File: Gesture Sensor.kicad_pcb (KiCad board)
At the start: 2 copper layers, 25.4 x 17.8 mm, 18 parts, among them J1 Conn_01x06_Male, J2 SM04B-SRSS-TB(LF)(SN), J3 SM04B-SRSS-TB(LF)(SN), U1 APDS-9960

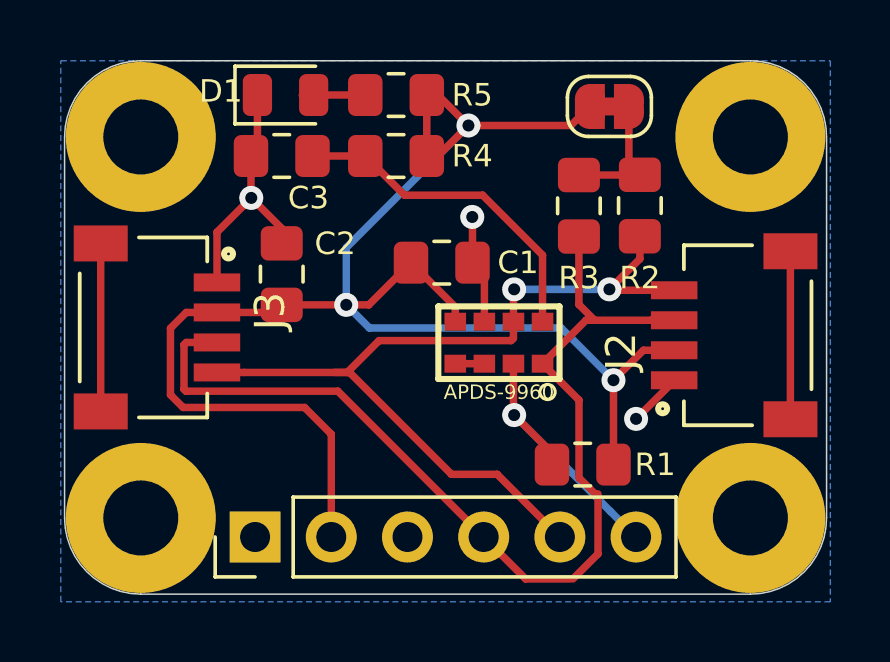
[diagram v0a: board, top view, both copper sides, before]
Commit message: Fixed schematic issue with Mosfet
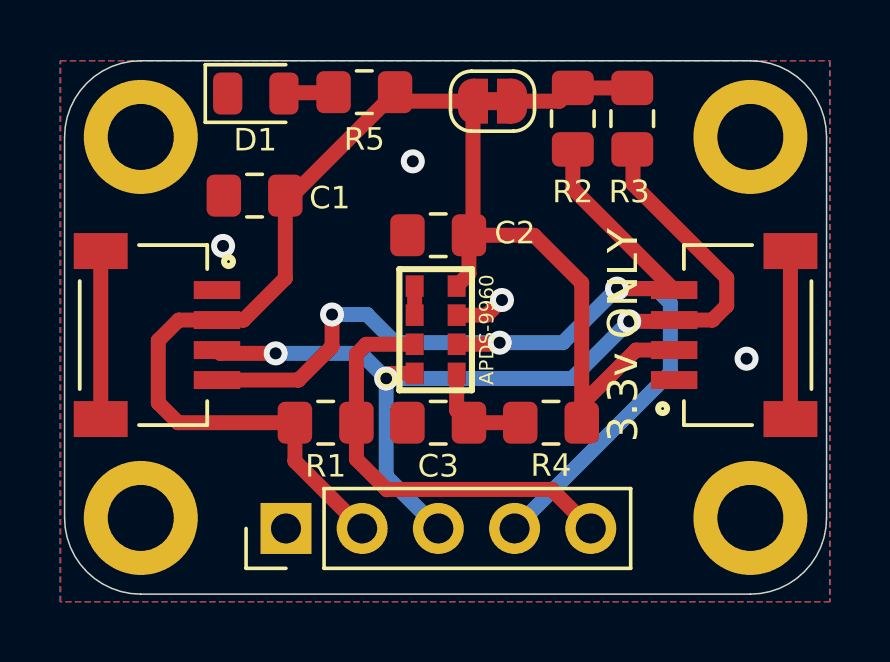
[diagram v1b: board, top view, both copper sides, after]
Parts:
- added G***: LOGO, Images:triplehorn_3-8_back_mask, F.Cu at (153.7, 54.1)
- added REF**: OSHW-Logo2_7.3x6mm_BackMask, Images:OSHW-Logo2_7.3x6mm_BackMask, F.Cu at (134.9, 55.4)
- H1, H2, H3, H4: footprint MountingHole:MountingHole_2.5mm_Pad -> MountingHole:MountingHole_2.2mm_M2_ISO14580_Pad
- J1: value Conn_01x06_Male -> Conn_01x05_Male; footprint Connector_PinHeader_2.54mm:PinHeader_1x06_P2.54mm_Vertical -> Connector_PinHeader_2.54mm:PinHeader_1x05_P2.54mm_Vertical
- moved C3 10.3 mm to (143.3, 57.8)
- moved R4 10.3 mm to (147.0, 57.8)
- moved R1 8.68 mm to (139.5, 57.8), turned to 0 degrees
- moved C1 6.63 mm to (137.1, 50.2), turned to 180 degrees
- moved C2 5.37 mm to (143.3, 51.5), turned to 180 degrees
- moved JP1 3.90 mm to (145.1, 47.1), turned to 180 degrees
- moved R2 3.66 mm to (147.8, 47.7)
- moved R3 3.41 mm to (149.7, 47.7)
- moved U1 2.15 mm to (143.2, 54.7), turned to 180 degrees
- moved J1 1.07 mm to (138.2, 61.3)
- moved R5 1.06 mm to (140.8, 46.8)
- moved D1 0.99 mm to (137.2, 46.8)
- moved J3 0.25 mm to (135.9, 54.9)
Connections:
- net Net-(C3-Pad1) renamed /VDD
- net Net-(U1-Pad3) renamed /LDR
- J1 pad 1: (no net) -> GND
- J1 pad 3: GND -> SDA
- J1 pad 4: SDA -> SCL
- J1 pad 5: SCL -> INT
- JP1 pad 1: +3V3 -> Net-(JP1-Pad1)
- JP1 pad 2: Net-(JP1-Pad2) -> +3V3
- R2 pad 1: Net-(JP1-Pad2) -> Net-(JP1-Pad1)
- R3 pad 1: Net-(JP1-Pad2) -> Net-(JP1-Pad1)
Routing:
- net GND: track 14.8 -> 1.72 mm, vias 3 -> 4
- net +3V3: track 55.9 -> 47.0 mm, vias 3 -> 0
- net /VDD: track 11.3 -> 3.52 mm
- net SCL: track 29.5 -> 37.1 mm, vias 2 -> 3
- net INT: track 9.64 -> 14.4 mm, vias 1 -> 0
- net Net-(JP1-Pad2): track 4.46 -> 0.00 mm
- net Net-(JP1-Pad1): track 0.00 -> 4.22 mm
- net SDA: track 34.3 -> 31.6 mm, vias 0 -> 3
- added copper zone on F.Cu, net GND
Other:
- board text added: "3.3v ONLY"
- board text added: "APDS 9960 Digital Proximity, Ambient Light, RGB and Gesture Sensor"
- board text added: "I2C Addr: 0x39"
- board text added: "v1 9/2020"
